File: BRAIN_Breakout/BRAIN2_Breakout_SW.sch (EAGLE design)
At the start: 101 parts

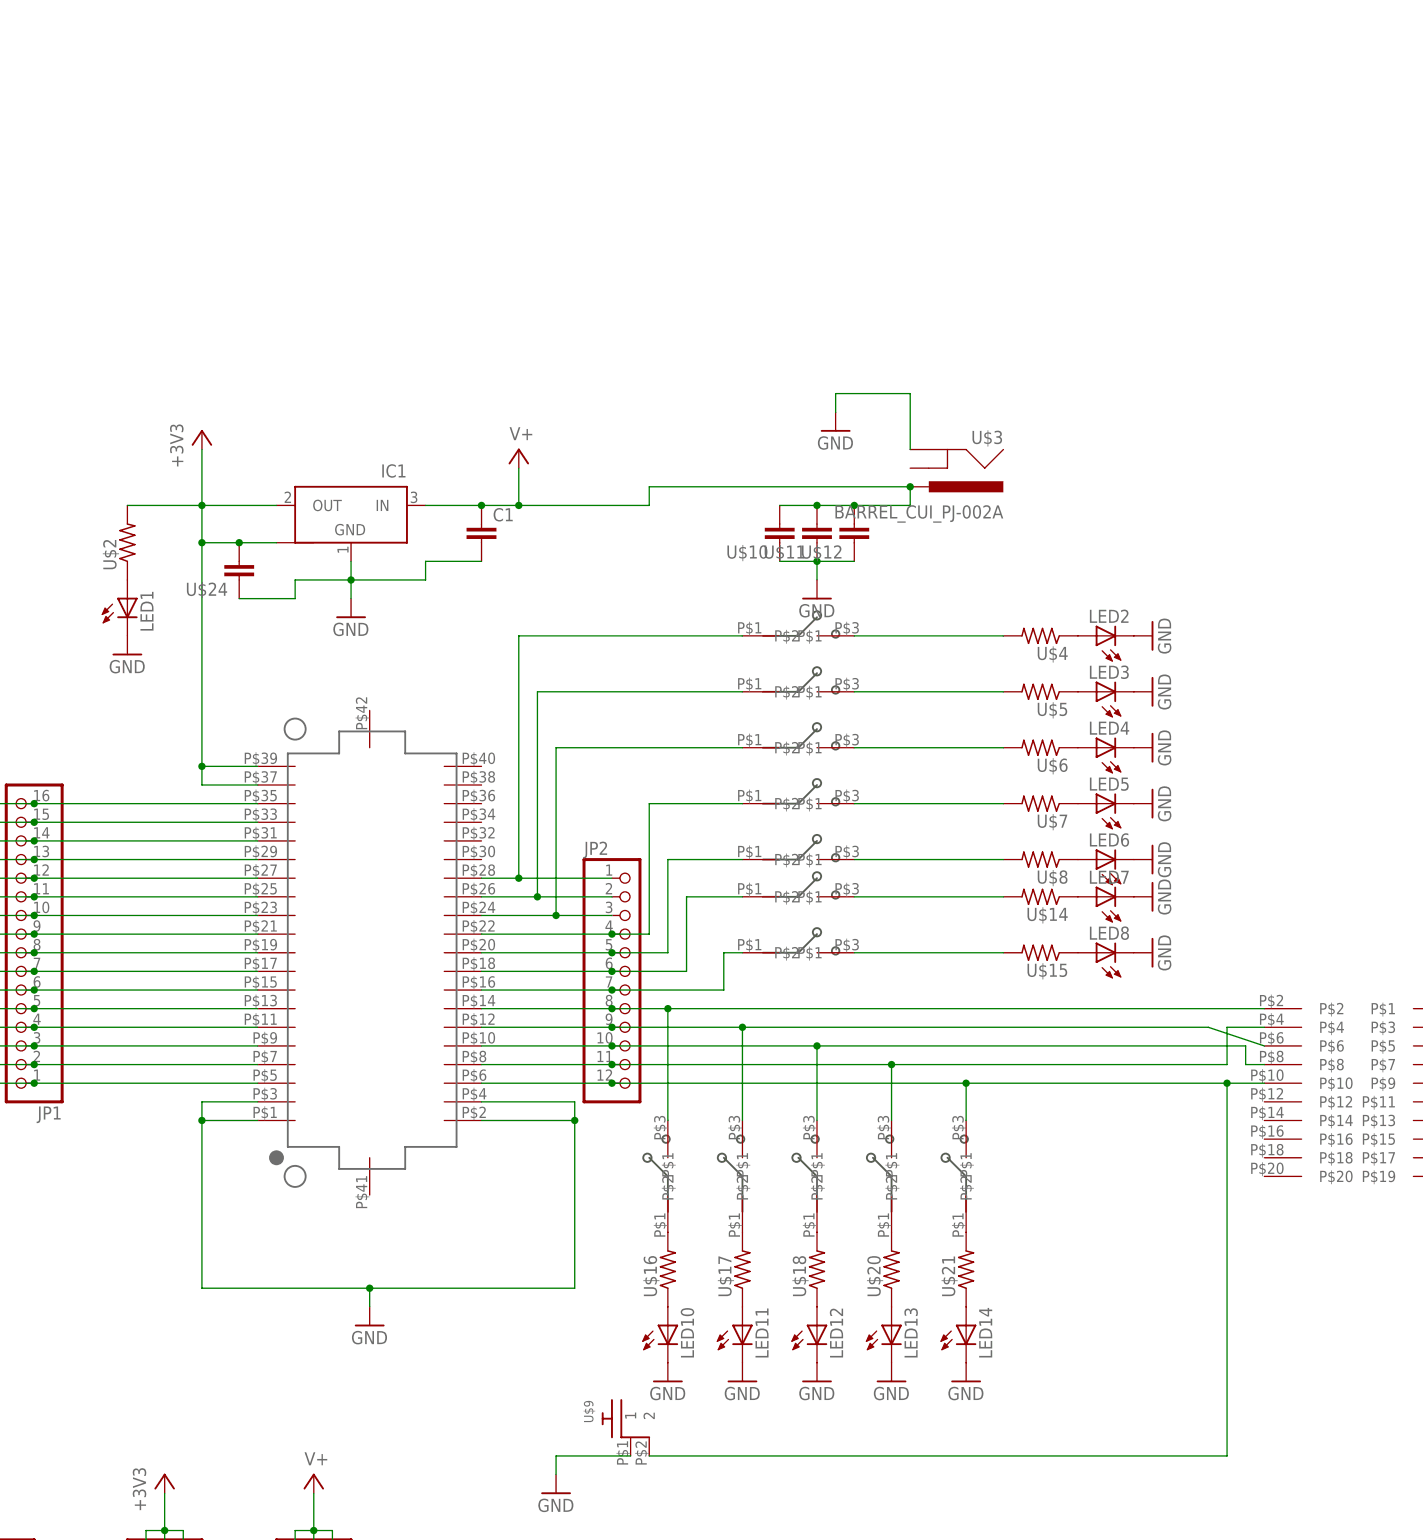
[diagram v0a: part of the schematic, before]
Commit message: Added board for new KW2
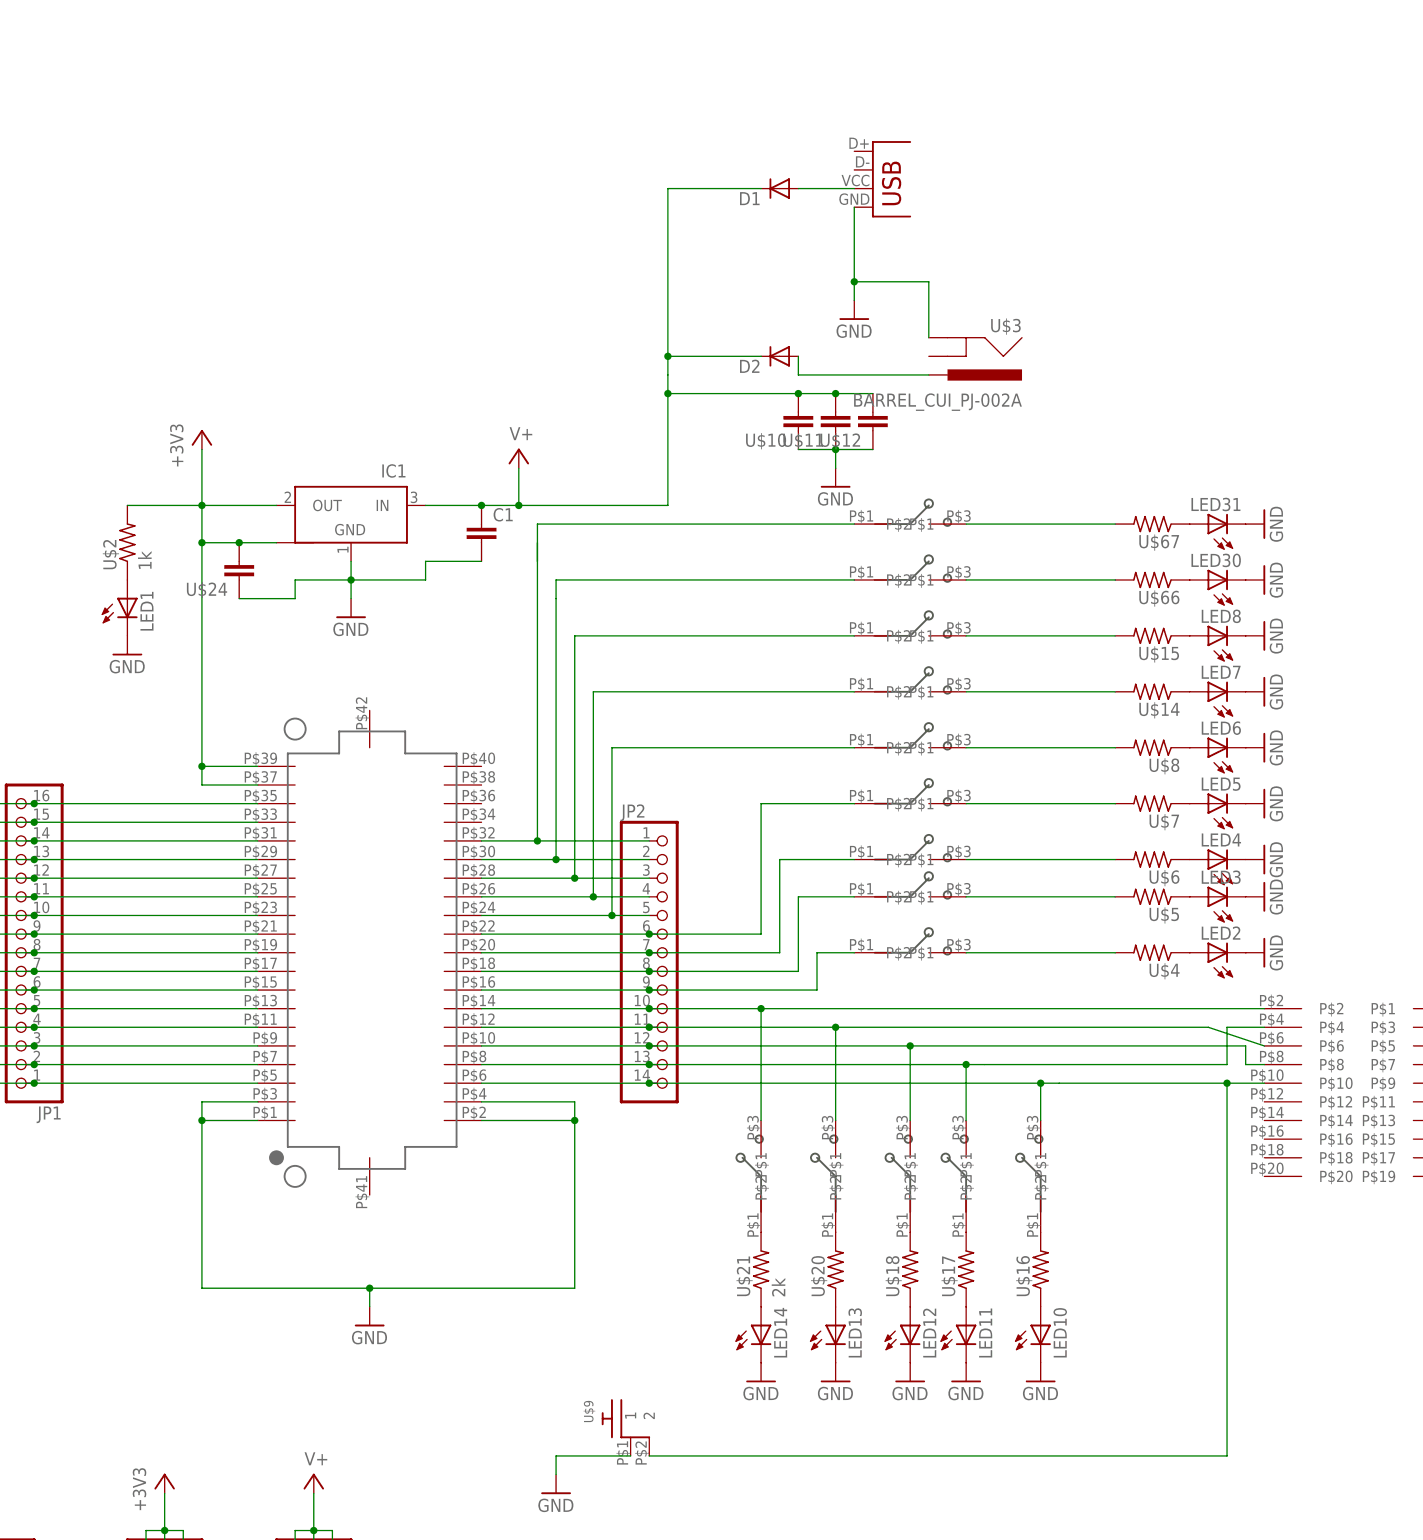
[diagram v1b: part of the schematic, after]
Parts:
- added D1, D2: (no value), SparkFun:DIODESMA
- added LED30, LED31: (no value), adafruit:LEDCHIP-LED0805
- added U$66, U$67: (no value), GW-devices:RF-R0805
- added U$68, U$69: CJS, KW2:CJS
- added X1: USB, SparkFun:USB
- C1, U$12, U$24: MFGN (none) -> Murata; MFGP (none) -> GRM219R61E106KA12D
- JP1: MFGN (none) -> Sullins Connector; MFGP (none) -> PRPC016SAAN-RC
- JP2: device pinhead:PINHD-1X12 -> pinhead:PINHD-1X14; MFGN (none) -> Sullins Connector; MFGP (none) -> PRPC012SAAN-RC
- JP3, JP4, JP5: MFGN (none) -> Sullins Connector; MFGP (none) -> PRPC003SAAN-RC
- LED1: MFGN (none) -> Wurth Electronics Inc; MFGP (none) -> 150080BS75000
- U$1: value DF12_F -> KW2_CPU_NEW; device KW2:DF12_F -> KW2:KW2_CPU_NEW; MFGN (none) -> Hirose; MFGP (none) -> DF12(3.0)-40DP-0.5V(86)
- U$10: MFGN (none) -> TDK; MFGP (none) -> C2012X5R1H104K085AA
- U$11: MFGN (none) -> TDK; MFGP (none) -> C2012X5R1E105K125AA
- U$13, U$14, U$15, U$16, U$17, U$18, U$20, U$22, U$23, U$25, U$26, U$27, U$28, U$29, U$30, U$31, U$32, U$33, U$34, U$35, U$36, U$37, U$4, U$5, U$6, U$7, U$8: MFGN (none) -> Panasonic; MFGP (none) -> ERJ-6ENF2001V
- U$19: MFGN (none) -> CNC Tech; MFGP (none) -> 3220-20-0100-00
- U$2: value (none) -> 1k; MFGN (none) -> Panasonic; MFGP (none) -> ERJ-6ENF2000V
- U$21: value (none) -> 2k; MFGN (none) -> Panasonic; MFGP (none) -> ERJ-6ENF2001V
- U$3: MFGN (none) -> CUI; MFGP (none) -> PJ002-A
- U$38, U$39, U$40, U$41, U$42, U$43, U$44, U$45, U$46, U$47, U$48, U$49, U$50, U$51, U$52, U$53, U$54, U$55, U$56, U$57, U$58, U$59, U$60, U$61, U$62, U$63, U$64, U$65: MFGN (none) -> Copal Electronics Inc; MFGP (none) -> CJS-1200TA
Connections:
- removed net N$51: JP2.9, U$1.PTA2/JTAG_TDO/TRACE?SWO/EZP_DO/UART0_TX/FTM0_CH7, U$19.P$6, U$55.P$2
- new net N$71: D2.A, U$3.PWR
- new net N$72: D1.A, X1.VBUS
- new net N$73: JP2.1, U$1.NC@3, U$69.P$1
- new net N$75: LED30.A, U$66.1
- new net N$76: LED31.A, U$67.1
- new net N$77: U$67.2, U$69.P$2
- new net N$78: U$66.2, U$68.P$2
- new net N$80: JP2.2, U$1.NC@4, U$68.P$1
- new net N$86: JP2.11, U$1.PTA2/JTAG_TDO/TRACE?SWO/EZP_DO/UART0_TX/FTM0_CH7, U$19.P$6, U$57.P$2
- net GND: now also LED30.C, LED31.C, X1.GND
- net N$21: now also JP2.3, U$65.P$1; no longer JP2.1, U$59.P$1
- net N$22: now also JP2.4, U$64.P$1; no longer JP2.2, U$60.P$1
- net N$23: now also JP2.5, U$63.P$1; no longer JP2.3, U$61.P$1
- net N$24: now also JP2.6; no longer JP2.4
- net N$25: now also JP2.7, U$61.P$1; no longer JP2.5, U$63.P$1
- net N$26: now also JP2.8, U$60.P$1; no longer JP2.6, U$64.P$1
- net N$27: now also JP2.9, U$59.P$1; no longer JP2.7, U$65.P$1
- net N$48: now also JP2.10, U$58.P$2; no longer JP2.8, U$54.P$2
- net N$54: now also JP2.12; no longer JP2.10
- net N$57: now also JP2.13, U$55.P$2; no longer JP2.11, U$57.P$2
- net N$60: now also JP2.14, U$54.P$2; no longer JP2.12, U$58.P$2
- net V+: now also D1.C, D2.C; no longer U$3.PWR
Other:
- moved on the sheet: LED10, LED11, LED12, LED13, LED14, LED2, LED3, LED4, LED5, LED6, LED7, LED8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
